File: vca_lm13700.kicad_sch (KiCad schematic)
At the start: 42 parts, among them Q201 Q_PNP_BEC, Q202 Q_PNP_BEC, U201 LM13700, U202 TL972, U203 TL072

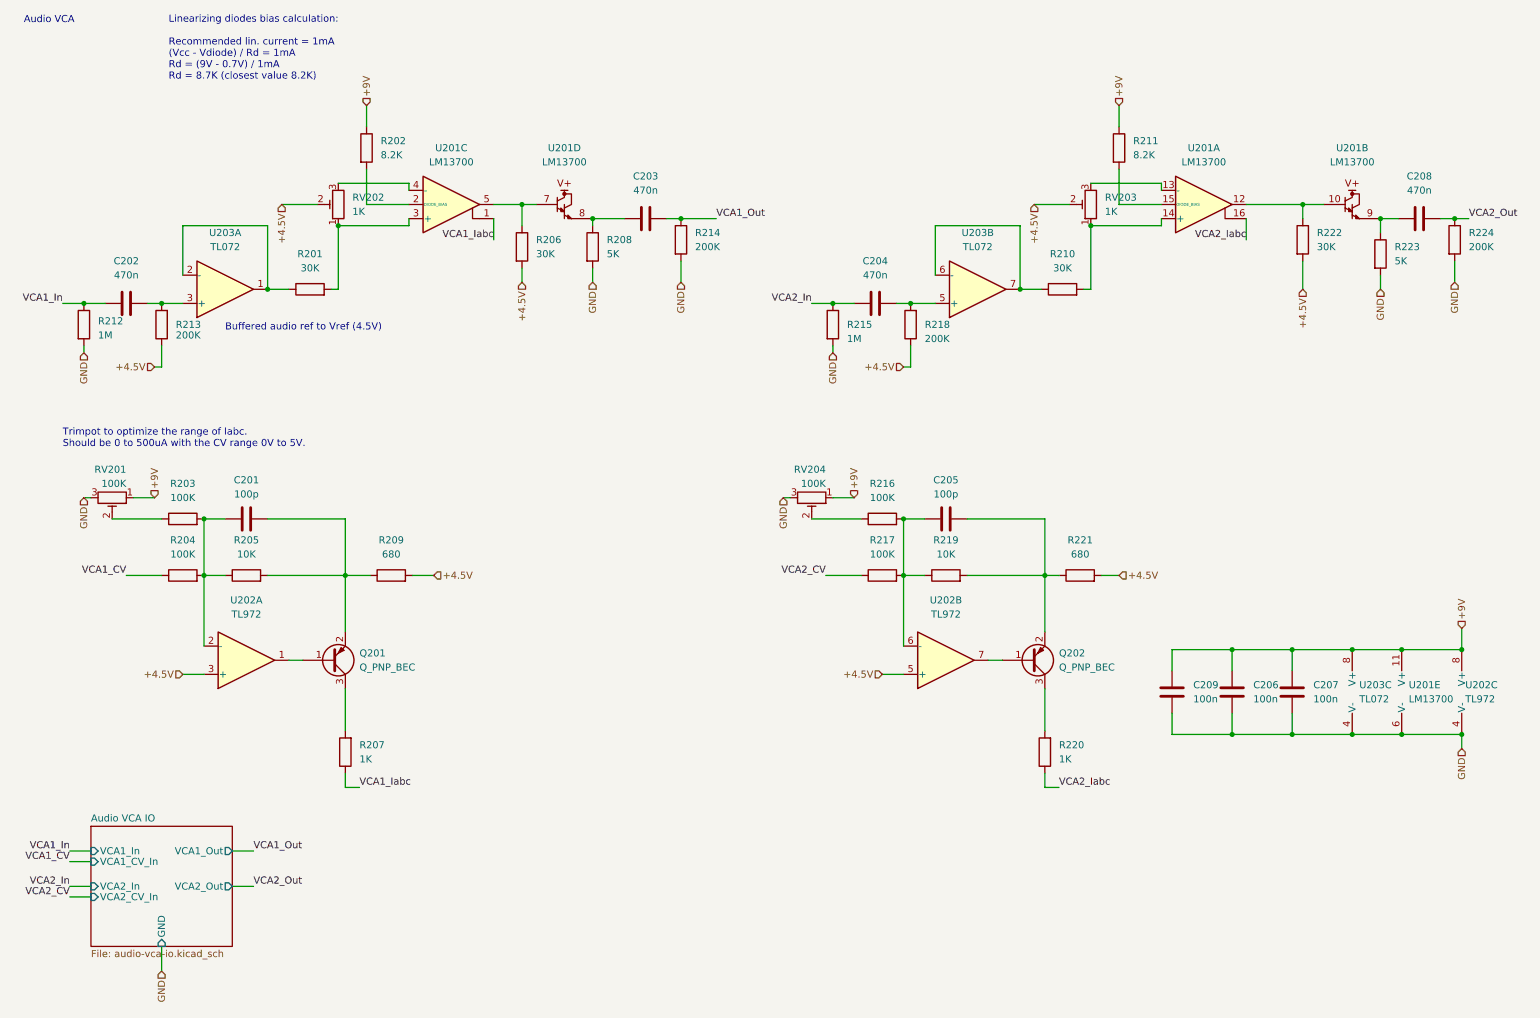
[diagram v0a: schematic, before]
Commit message: Add JLC parts numbers
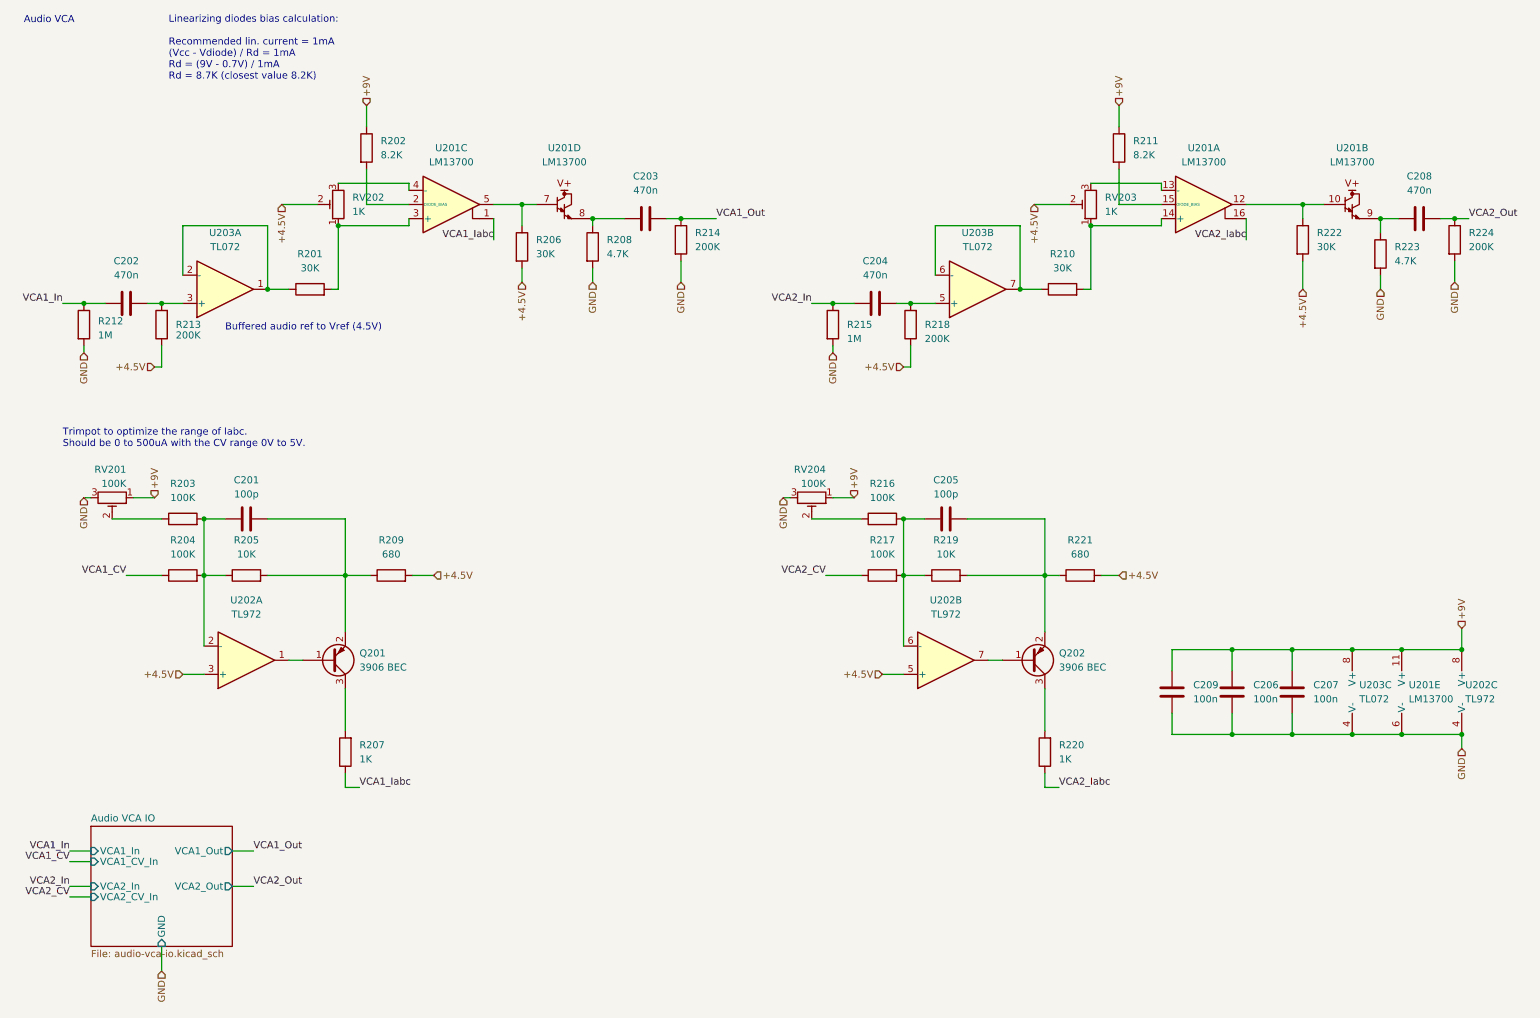
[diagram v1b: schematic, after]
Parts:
- C201, C205: LCSC (none) -> C160903; Role (none) -> opamp-filter
- C202, C203, C204, C208: LCSC (none) -> C651004; Role (none) -> audio-coupling
- C206, C207, C209: LCSC (none) -> C497032; Role (none) -> ic-bypass
- Q201, Q202: value Q_PNP_BEC -> 3906 BEC; LCSC (none) -> C2891809
- R201, R206, R210, R222: LCSC (none) -> C2907025
- R202, R211: LCSC (none) -> C188034
- R203, R204, R216, R217: LCSC (none) -> C14675
- R205, R219: LCSC (none) -> C98220
- R207, R220: LCSC (none) -> C2907002
- R208, R223: value 5K -> 4.7K; LCSC (none) -> C103656
- R209, R221: LCSC (none) -> C328372
- R212, R215: LCSC (none) -> C234360
- R213, R214, R218, R224: LCSC (none) -> C203392
- RV201, RV204: LCSC (none) -> C51284
- RV202, RV203: LCSC (none) -> C124615
- U201: LCSC (none) -> C174050
- U202: LCSC (none) -> C46127
- U203: LCSC (none) -> C67473
